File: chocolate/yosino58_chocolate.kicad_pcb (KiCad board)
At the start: 2 copper layers, 156.8 x 135 mm, 121 parts, among them J0 LED, J1 TRRS, J2 OLED, J3 OLED, J4 OLED, J5 OLED, J6 OLED, P1 i2c_pin, P2 i2c_pin, SW1 SW_PUSH, SW10 SW_PUSH, SW11 SW_PUSH, SW12 SW_PUSH, SW13 SW_PUSH, SW14 SW_PUSH, SW15 SW_PUSH, SW16 SW_PUSH, SW17 SW_PUSH, SW18 SW_PUSH, SW19 SW_PUSH, SW2 SW_PUSH, SW20 SW_PUSH, SW21 SW_PUSH, SW22 SW_PUSH, SW23 SW_PUSH, SW24 SW_PUSH, SW25 SW_PUSH, SW26 SW_PUSH, SW27 SW_PUSH, SW28 SW_PUSH, SW29 SW_PUSH, SW3 SW_PUSH, SW4 SW_PUSH, SW5 SW_PUSH, SW6 SW_PUSH, SW7 SW_PUSH, SW8 SW_PUSH, SW9 SW_PUSH, U1 ProMicro, U2 ProMicro

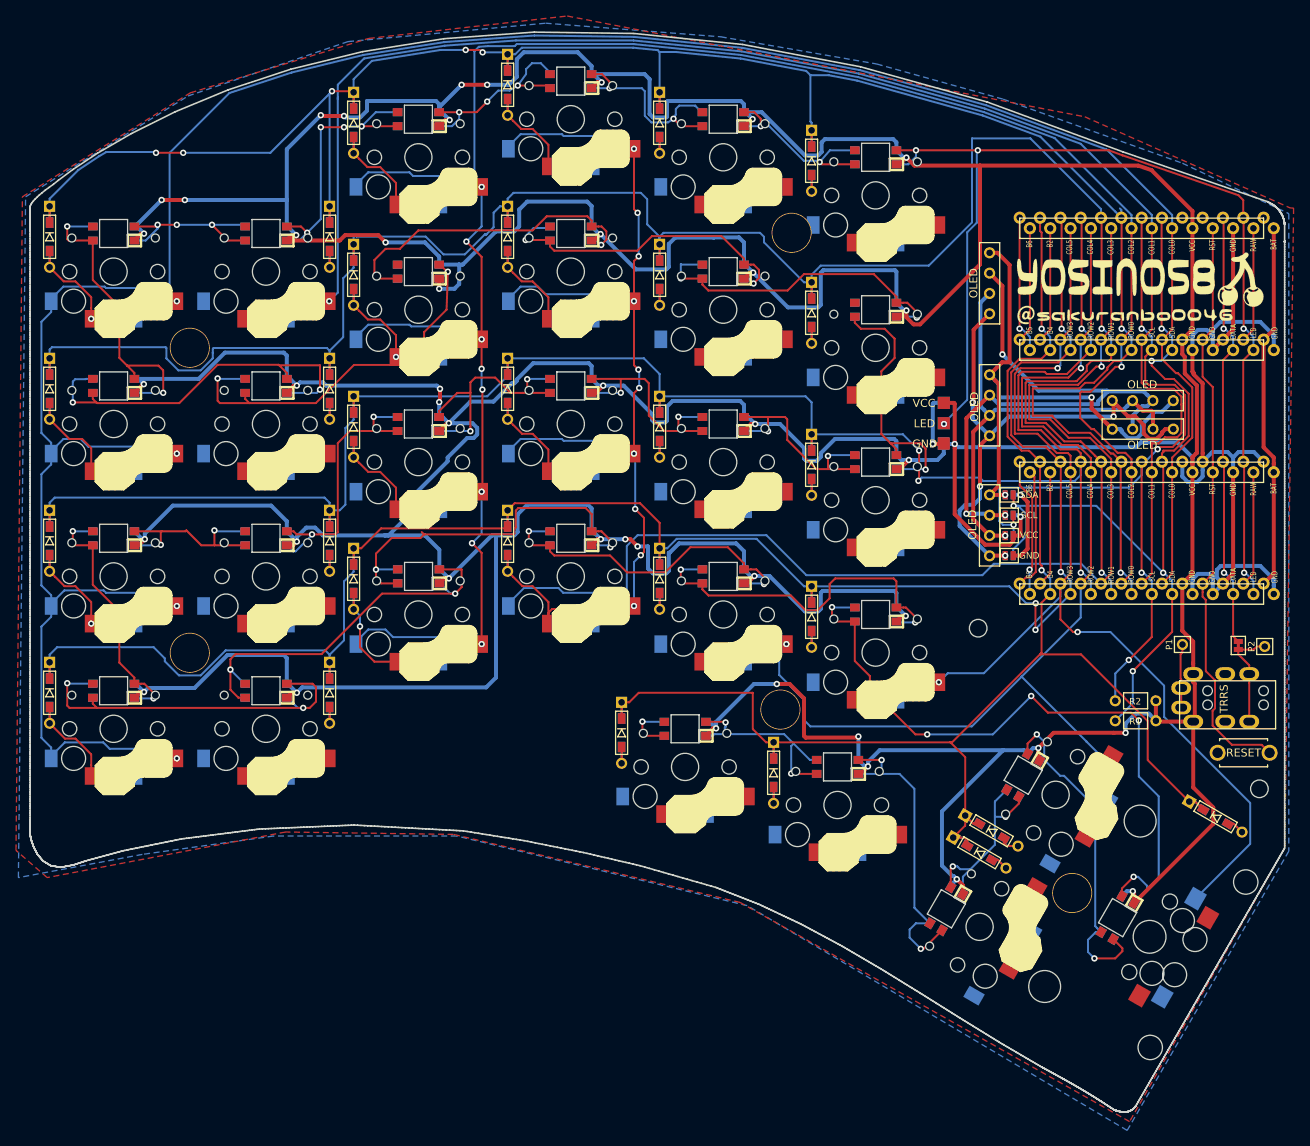
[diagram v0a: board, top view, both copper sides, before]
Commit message: ソケット版追加
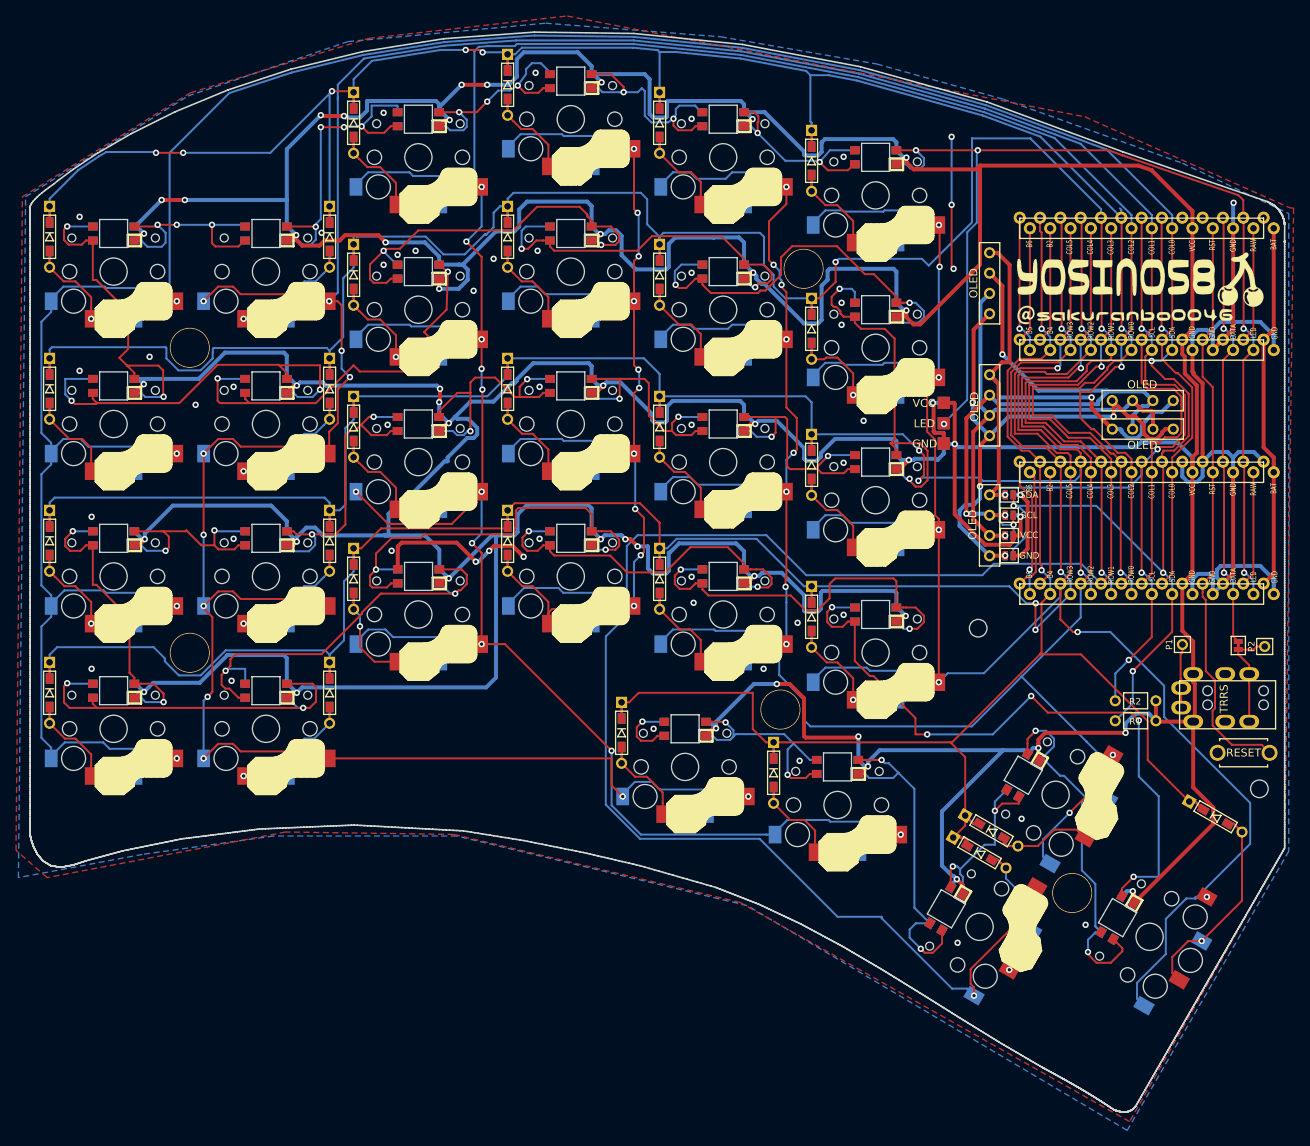
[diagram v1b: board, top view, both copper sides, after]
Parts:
- L1, L10, L11, L12, L13, L14, L15, L16, L17, L18, L19, L2, L20, L21, L22, L23, L24, L25, L26, L27, L28, L29, L3, L4, L5, L6, L7, L8, L9: footprint yosino58_chocolate:SK6812MINI_padin_rev -> yosino58_chocolate:SK6812MINI_rev
- SW29: footprint yosino58_chocolate:CherryMX_Hotswap2U_stabilizer. -> yosino58_chocolate:Choc_Hotswap2U_stabilizer
- moved Ref** 4.74 mm to (136.8, 52.0)
- moved D12 2.00 mm to (137.8, 59.5)
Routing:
- net col1: track 190.5 -> 382.5 mm, vias 1 -> 11
- net col4: track 128.5 -> 281.4 mm, vias 2 -> 11
- net col5: track 131.9 -> 281.1 mm, vias 3 -> 8
- net col3: track 262.9 -> 363.4 mm, vias 11 -> 12
- net col2: track 272.8 -> 360.1 mm, vias 9 -> 12
- net GND: track 119.8 -> 160.9 mm, vias 2 -> 51
- net Net-(D29-Pad2): track 4.37 -> 27.8 mm, vias 0 -> 1
- net Net-(D27-Pad2): track 4.37 -> 23.0 mm, vias 0 -> 1
- net Net-(D6-Pad2): track 4.07 -> 21.0 mm, vias 0 -> 1
- net Net-(D5-Pad2): track 4.07 -> 20.9 mm, vias 0 -> 1
- net Net-(D24-Pad2): track 4.07 -> 20.9 mm, vias 0 -> 1
- net Net-(D11-Pad2): track 4.07 -> 20.9 mm, vias 0 -> 1
- net Net-(D18-Pad2): track 4.07 -> 20.8 mm, vias 0 -> 1
- net Net-(D20-Pad2): track 4.07 -> 20.8 mm, vias 0 -> 1
- net Net-(D23-Pad2): track 4.07 -> 20.8 mm, vias 0 -> 1
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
